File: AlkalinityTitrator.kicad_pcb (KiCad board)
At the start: 2 copper layers, 85 x 100 mm, 43 parts, among them J1 Conn_01x16, J10 Screw_Terminal_01x02, J14 Conn_01x02, J2 Raspberry_Pi_2_3, J3 Conn_01x08, J4 Screw_Terminal_01x04_titrator, J5 RF_Shield_Two_Pieces, J6 BNC_Jack, J7 SJ-43515TS, J8 Screw_Terminal_01x03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

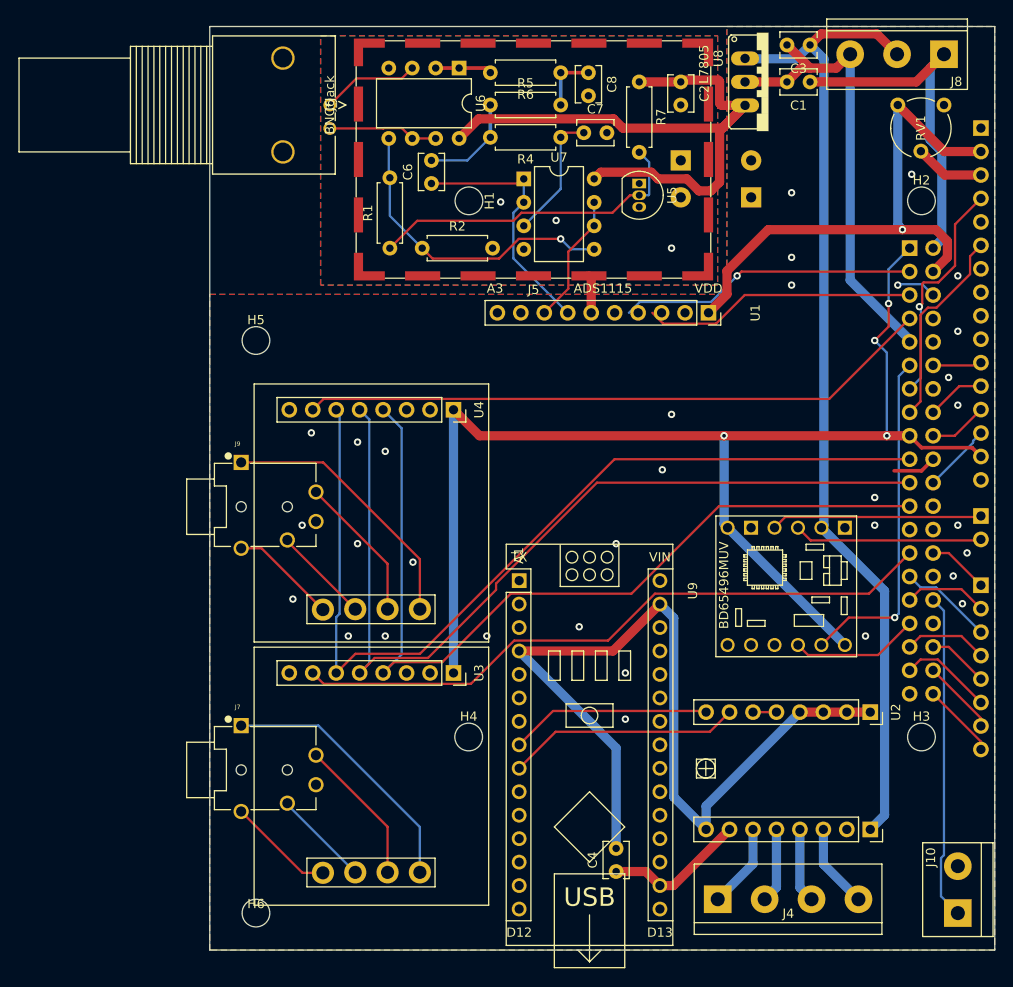
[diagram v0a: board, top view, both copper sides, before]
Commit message: Finished Rev3, added silkscreen, added voltage reference capacitors, generated gerbers and drills
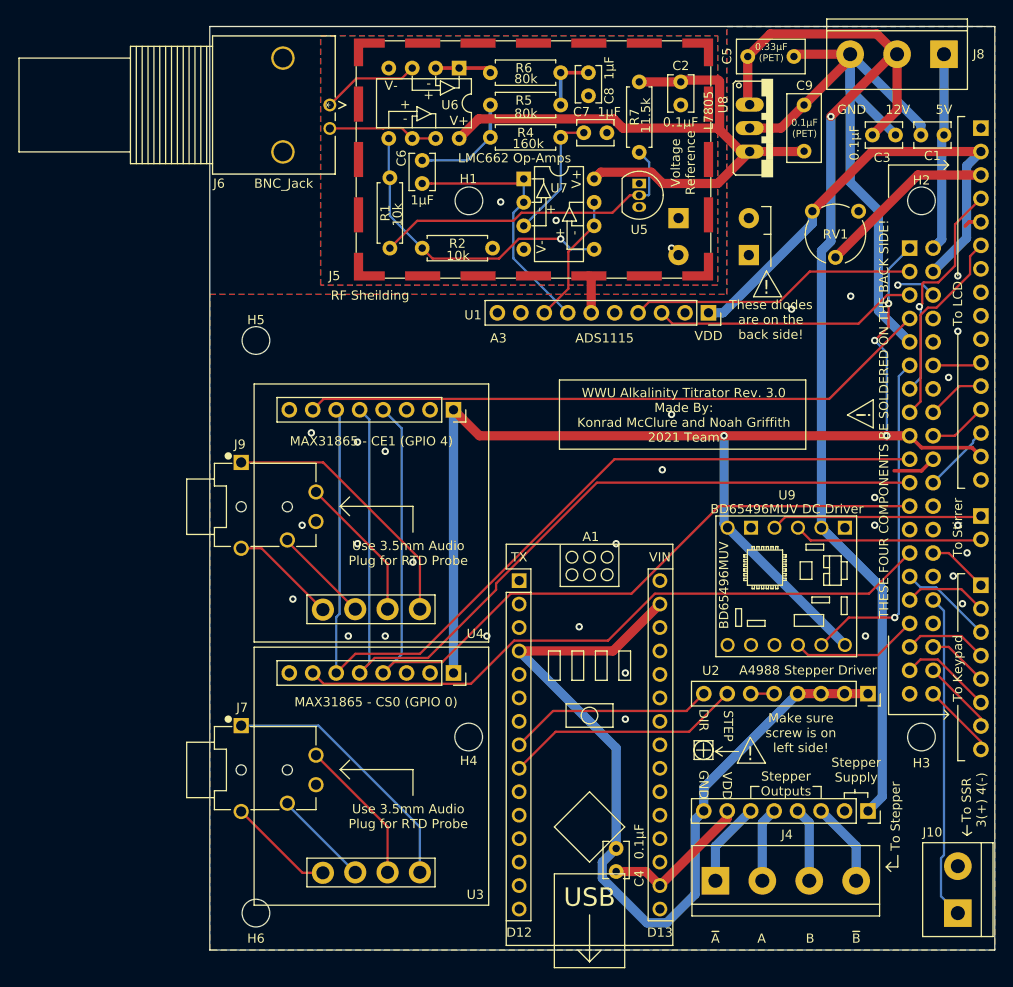
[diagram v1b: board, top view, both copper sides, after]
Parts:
- added C5: 0.33uF, Titrator_Footprints:C_Rect_L7.2mm_W3.5mm_P5.00mm_FKS2_FKP2_MKS2_MKP2, F.Cu at (179.8, 45.6)
- added C9: 0.1uF, Titrator_Footprints:C_Rect_L7.2mm_W3.5mm_P5.00mm_FKS2_FKP2_MKS2_MKP2, F.Cu at (185.9, 55.9)
- moved C1 15.6 mm to (201.1, 54.1)
- moved RV1 14.8 mm to (186.8, 62.4)
- moved C3 11.9 mm to (193.3, 54.1), turned to 0 degrees
- moved D2 6.25 mm to (180.0, 67.1)
- moved D1 6.25 mm to (172.3, 63.1)
- moved U8 5.02 mm to (182.6, 53.4)
- moved J4 2.02 mm to (176.3, 134.9)
- moved U2 2.02 mm to (193.3, 114.4)
- moved C6 1.00 mm to (144.6, 59.4)
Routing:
- net /PSU_GND: track 50.0 -> 77.6 mm
- net /PSU_5V: track 38.3 -> 21.5 mm
- net /PSU_12V: track 107.7 -> 122.2 mm, vias 0 -> 1
- net /LCD_OV: track 7.57 -> 19.4 mm
- net +5V: track 60.3 -> 52.7 mm, vias 1 -> 0
- net GND: track 9.09 -> 11.0 mm, vias 32 -> 29
- net /Arduino_VDD: track 15.4 -> 16.5 mm
- net Net-(C6-Pad2): track 10.9 -> 11.9 mm
- net Net-(C6-Pad1): track 27.6 -> 28.6 mm
- net /SDA: track 32.3 -> 31.3 mm, vias 1 -> 0
- net /SCL: track 29.6 -> 28.9 mm
- net /STEP: track 25.3 -> 25.9 mm
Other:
- board text added: "!"
- board text added: "+"
- board text added: "-"
- board text added: "0.1μF"
- board text added: "0.1μF (PET)"
- board text added: "0.33μF (PET)"
- board text added: "10k"
- board text added: "11.5k"
- board text added: "12V"
- board text added: "160k"
- board text added: "1μF"
- board text added: "5V"
- board text added: "80k"
- board text added: "A"
- board text added: "A4988 Stepper Driver"
- board text added: "B"
- board text added: "DIR"
- board text added: "GND"
- board text added: "LMC662 Op-Amps"
- board text added: "MAX31865 - CE1 (GPIO 4)"
- board text added: "MAX31865 - CS0 (GPIO 0)"
- board text added: "Make sure screw is on left side!"
- board text added: "RF Sheilding"
- board text added: "STEP"
- board text added: "Schottky Diodes For Connecting GND Planes"
- board text added: "Stepper Outputs"
- board text added: "Stepper Supply"
- board text added: "THESE FOUR COMPONENTS BE SOLDERED ON THE BACK SIDE!"
- board text added: "These diodes are on the back side!"
- board text added: "To Keypad"
- board text added: "To LCD"
- board text added: "To SSR 3(+) 4(-)"
- board text added: "To Stepper"
- board text added: "To Stirrer"
- board text added: "Use 3.5mm Audio Plug for RTD Probe"
- board text added: "V+"
- board text added: "V-"
- board text added: "VDD"
- board text added: "Voltage Reference"
- board text added: "WWU Alkalinity Titrator Rev. 3.0 Made By: Konrad McClure and Noah Griffith 2021 Team"
- board text added: "~A~"
- board text added: "~B~"
